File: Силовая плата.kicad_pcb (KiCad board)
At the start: 2 copper layers, 75 x 75 mm, 9 parts, among them Q1 BSP89, Q2 BSP89, Q3 BSP89, Q4 BSP89, Q5 BSP89, Q6 BSP89, U1 HIP2100_SOIC, U2 HIP2100_SOIC, U3 HIP2100_SOIC

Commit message: Вариант с транзисторами в линию
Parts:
- U1, U2, U3: footprint Package_DFN_QFN:DFN-8-1EP_3x3mm_P0.5mm_EP1.65x2.38mm -> Package_SO:SOIC-8_3.9x4.9mm_P1.27mm
- moved U1 118.7 mm to (180.3, 100.3), turned to 90 degrees
- moved U2 90.1 mm to (154.3, 100.3)
- moved U3 75.4 mm to (127.6, 100.3)
- moved Q1 12.3 mm to (133.1, 86.2), turned to -90 degrees
- moved Q3 10.9 mm to (158.1, 86.4), turned to -90 degrees
- moved Q5 10.0 mm to (182.0, 86.2), turned to -90 degrees
- moved Q6 9.01 mm to (170.2, 82.5), turned to 90 degrees
- moved Q4 7.75 mm to (146.1, 82.5), turned to 90 degrees
- moved Q2 6.22 mm to (121.0, 82.5), turned to 90 degrees
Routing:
- net G3: track 0.00 -> 28.1 mm, vias 0 -> 1
- net G1: track 0.00 -> 27.9 mm, vias 0 -> 1
- net G5: track 0.00 -> 24.8 mm, vias 0 -> 1
- net G6: track 0.00 -> 20.0 mm, vias 0 -> 1
- net G4: track 0.00 -> 18.5 mm, vias 0 -> 1
- net G2: track 0.00 -> 17.9 mm, vias 0 -> 1
- net C: vias 0 -> 12
- net B: vias 0 -> 12
- net A: vias 0 -> 12
- net +12V: vias 0 -> 11
- added copper zone on B.Cu, net +12V
- added copper zone on B.Cu, net A
- added copper zone on In1.Cu, net A
- added copper zone on In2.Cu, net A
- added copper zone on In3.Cu, net A
- added copper zone on In4.Cu, net A
- added copper zone on B.Cu, net B
- added copper zone on F.Cu, net B
- added copper zone on In1.Cu, net B
- added copper zone on In2.Cu, net B
- added copper zone on In3.Cu, net B
- added copper zone on In4.Cu, net B
- added copper zone on B.Cu, net C
- added copper zone on F.Cu, net C
- added copper zone on In1.Cu, net C
- added copper zone on In2.Cu, net C
- added copper zone on In3.Cu, net C
- added copper zone on In4.Cu, net C
- added copper zone on In1.Cu, net GND
- added copper zone on In2.Cu, net GND
- added copper zone on In3.Cu, net GND
- added copper zone on In4.Cu, net GND
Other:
- copper layers 2 -> 6

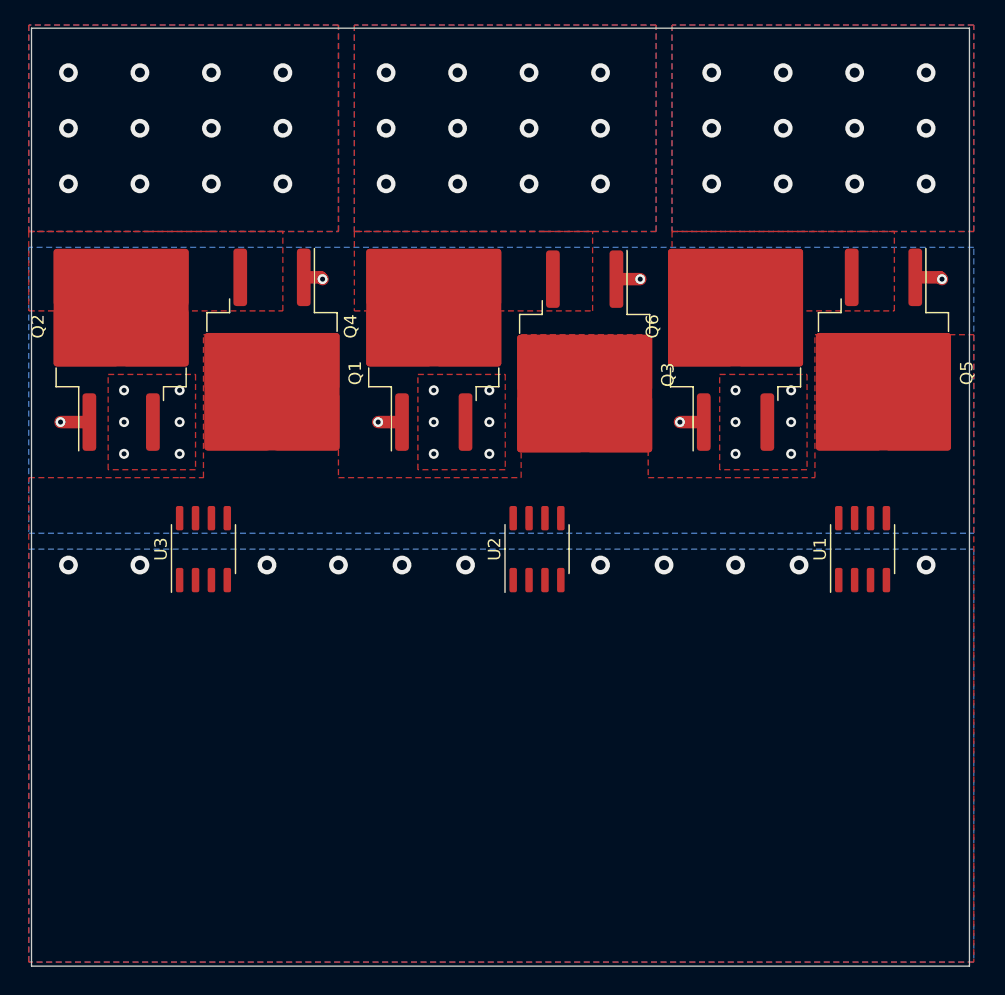
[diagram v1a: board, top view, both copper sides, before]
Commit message: Добавил датчики тока и шунты
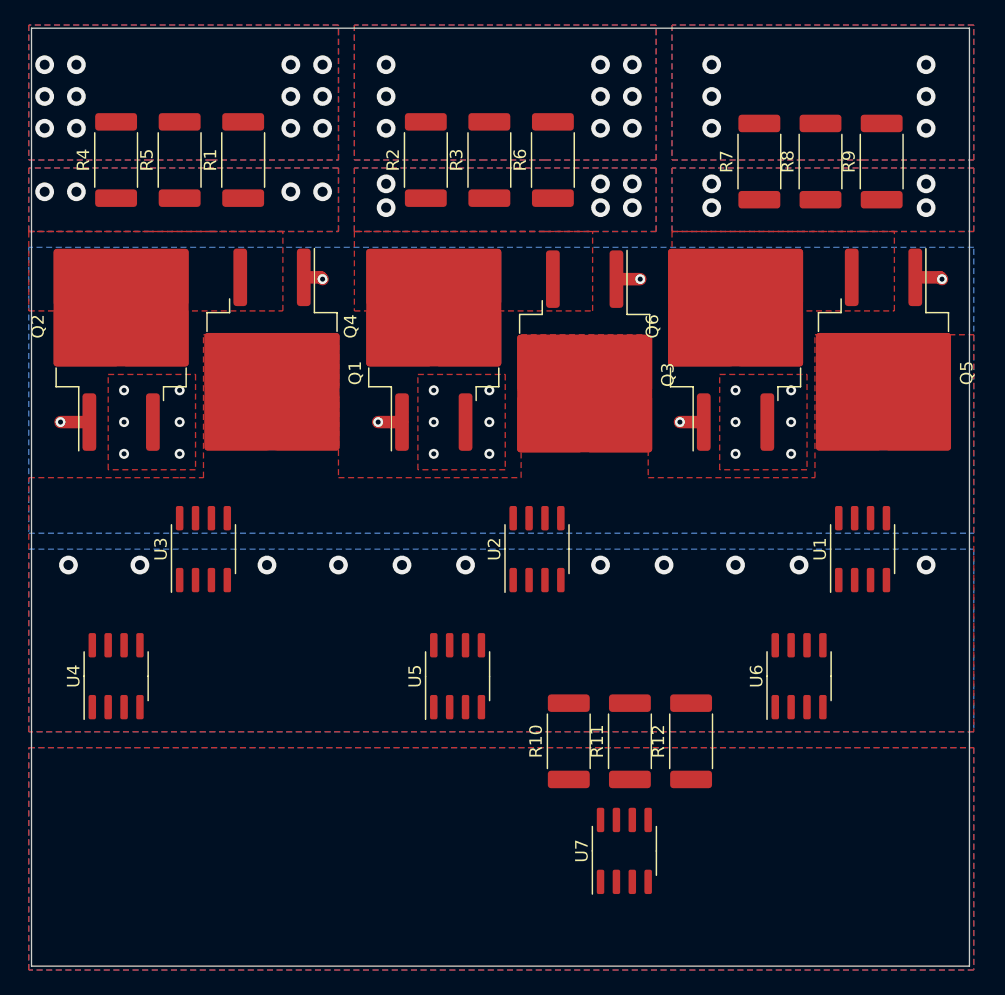
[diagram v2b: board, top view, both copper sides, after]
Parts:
- added R1: R, Resistor_SMD:R_2512_6332Metric_Pad1.40x3.35mm_HandSolder, F.Cu at (130.8, 69.2)
- added R10: R, Resistor_SMD:R_2512_6332Metric_Pad1.40x3.35mm_HandSolder, F.Cu at (156.8, 115.7)
- added R11: R, Resistor_SMD:R_2512_6332Metric_Pad1.40x3.35mm_HandSolder, F.Cu at (161.7, 115.7)
- added R12: R, Resistor_SMD:R_2512_6332Metric_Pad1.40x3.35mm_HandSolder, F.Cu at (166.6, 115.7)
- added R2: R, Resistor_SMD:R_2512_6332Metric_Pad1.40x3.35mm_HandSolder, F.Cu at (145.4, 69.2)
- added R3: R, Resistor_SMD:R_2512_6332Metric_Pad1.40x3.35mm_HandSolder, F.Cu at (150.5, 69.2)
- added R4: R, Resistor_SMD:R_2512_6332Metric_Pad1.40x3.35mm_HandSolder, F.Cu at (120.7, 69.2)
- added R5: R, Resistor_SMD:R_2512_6332Metric_Pad1.40x3.35mm_HandSolder, F.Cu at (125.7, 69.2)
- added R6: R, Resistor_SMD:R_2512_6332Metric_Pad1.40x3.35mm_HandSolder, F.Cu at (155.6, 69.2)
- added R7: R, Resistor_SMD:R_2512_6332Metric_Pad1.40x3.35mm_HandSolder, F.Cu at (172.1, 69.3)
- added R8: R, Resistor_SMD:R_2512_6332Metric_Pad1.40x3.35mm_HandSolder, F.Cu at (177.0, 69.3)
- added R9: R, Resistor_SMD:R_2512_6332Metric_Pad1.40x3.35mm_HandSolder, F.Cu at (181.9, 69.3)
- added U4: AD8210, Package_SO:SOIC-8_3.9x4.9mm_P1.27mm, F.Cu at (120.7, 110.5)
- added U5: AD8210, Package_SO:SOIC-8_3.9x4.9mm_P1.27mm, F.Cu at (148.0, 110.5)
- added U6: AD8210, Package_SO:SOIC-8_3.9x4.9mm_P1.27mm, F.Cu at (175.3, 110.5)
- added U7: AD8210, Package_SO:SOIC-8_3.9x4.9mm_P1.27mm, F.Cu at (161.3, 124.5)
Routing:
- net A2: track 0.00 -> 57.3 mm, vias 0 -> 12
- net B2: track 0.00 -> 54.2 mm, vias 0 -> 9
- net C2: track 0.00 -> 52.0 mm, vias 0 -> 6
- net C: track 0.00 -> 37.0 mm, vias 12 -> 4
- net B: track 0.00 -> 35.9 mm, vias 12 -> 6
- net A: track 0.00 -> 34.2 mm, vias 12 -> 4
- added copper zone on B.Cu, net +12VA
- added copper zone on F.Cu, net +12VA
- added copper zone on B.Cu, net A2
- added copper zone on F.Cu, net A2
- added copper zone on In1.Cu, net A2
- added copper zone on In3.Cu, net A2
- added copper zone on In4.Cu, net A2
- added copper zone on B.Cu, net B2
- added copper zone on F.Cu, net B2
- added copper zone on In1.Cu, net B2
- added copper zone on In3.Cu, net B2
- added copper zone on In4.Cu, net B2
- added copper zone on B.Cu, net C2
- added copper zone on F.Cu, net C2
- added copper zone on In1.Cu, net C2
- added copper zone on In3.Cu, net C2
- added copper zone on In4.Cu, net C2
- removed copper zone on In2.Cu, net A
- removed copper zone on In2.Cu, net B
- removed copper zone on In2.Cu, net C

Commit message: Начальная версия
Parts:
- added C1: 1400m, Capacitor_THT:CP_Axial_L30.0mm_D18.0mm_P35.00mm_Horizontal, F.Cu at (110.8, 68.6)
- added C10: 0.1u, Capacitor_SMD:C_0805_2012Metric_Pad1.18x1.45mm_HandSolder, F.Cu at (47.4, 157.1)
- added C11: 0.1u, Capacitor_SMD:C_0805_2012Metric_Pad1.18x1.45mm_HandSolder, F.Cu at (47.4, 160.1)
- added C12: 0.1u, Capacitor_SMD:C_0805_2012Metric_Pad1.18x1.45mm_HandSolder, F.Cu at (47.4, 163.1)
- added C13: 0.1u, Capacitor_SMD:C_0805_2012Metric_Pad1.18x1.45mm_HandSolder, F.Cu at (47.4, 166.1)
- added C2: 1400m, Capacitor_THT:CP_Axial_L30.0mm_D18.0mm_P35.00mm_Horizontal, F.Cu at (111.0, 88.3)
- added C3: 1400m, Capacitor_THT:CP_Axial_L30.0mm_D18.0mm_P35.00mm_Horizontal, F.Cu at (111.0, 108.7)
- added C4: C_Small, Capacitor_SMD:C_0805_2012Metric_Pad1.18x1.45mm_HandSolder, F.Cu at (136.7, 108.6)
- added C5: BS, Capacitor_SMD:C_0805_2012Metric_Pad1.18x1.45mm_HandSolder, F.Cu at (123.2, 109.2)
- added C6: C_Small, Capacitor_SMD:C_0805_2012Metric_Pad1.18x1.45mm_HandSolder, F.Cu at (161.7, 108.6)
- added C7: BS, Capacitor_SMD:C_0805_2012Metric_Pad1.18x1.45mm_HandSolder, F.Cu at (148.2, 109.2)
- added C8: C_Small, Capacitor_SMD:C_0805_2012Metric_Pad1.18x1.45mm_HandSolder, F.Cu at (186.7, 108.8)
- added C9: BS, Capacitor_SMD:C_0805_2012Metric_Pad1.18x1.45mm_HandSolder, F.Cu at (173.2, 109.0)
- added D1: D_Small, Diode_SMD:D_SOD-323, F.Cu at (130.6, 113.0)
- added D2: D_Small, Diode_SMD:D_SOD-323, F.Cu at (155.6, 113.0)
- added D3: D_Small, Diode_SMD:D_SOD-323, F.Cu at (180.6, 113.2)
- added J6: 2-338069-0, Connector_My:2-338069-0, F.Cu at (138.4, 122.0)
- added R13: 2.7, Resistor_SMD:R_1206_3216Metric_Pad1.30x1.75mm_HandSolder, F.Cu at (117.5, 102.2)
- added R14: 2.7, Resistor_SMD:R_1206_3216Metric_Pad1.30x1.75mm_HandSolder, F.Cu at (123.2, 102.2)
- added R15: 2.7, Resistor_SMD:R_1206_3216Metric_Pad1.30x1.75mm_HandSolder, F.Cu at (142.5, 102.2)
- added R16: 2.7, Resistor_SMD:R_1206_3216Metric_Pad1.30x1.75mm_HandSolder, F.Cu at (148.2, 102.2)
- added R17: 2.7, Resistor_SMD:R_1206_3216Metric_Pad1.30x1.75mm_HandSolder, F.Cu at (167.5, 102.2)
- added R18: 2.7, Resistor_SMD:R_1206_3216Metric_Pad1.30x1.75mm_HandSolder, F.Cu at (173.2, 102.2)
- added R19: 10k, Resistor_SMD:R_0805_2012Metric_Pad1.20x1.40mm_HandSolder, F.Cu at (52.2, 157.1)
- added R20: 10k, Resistor_SMD:R_0805_2012Metric_Pad1.20x1.40mm_HandSolder, F.Cu at (52.2, 160.0)
- U1, U2, U3: value HIP2100_SOIC -> IRS21867S
- moved R3 131.1 mm to (83.8, 182.1)
- moved R4 131.1 mm to (54.0, 182.1)
- moved R5 131.1 mm to (59.1, 182.1)
- moved R7 131.1 mm to (105.4, 182.2)
- moved R9 131.1 mm to (115.2, 182.2)
- moved R1 131.1 mm to (64.1, 182.1)
- moved R2 131.1 mm to (78.7, 182.1)
- moved R6 131.1 mm to (88.9, 182.1)
- moved R8 131.1 mm to (110.3, 182.2)
- moved U3 53.5 mm to (180.4, 108.8), turned to 180 degrees
- moved U1 50.6 mm to (130.4, 108.6), turned to 180 degrees
- moved R10 44.3 mm to (129.5, 150.6)
- moved R11 44.3 mm to (134.4, 150.6)
- moved R12 44.3 mm to (139.3, 150.6)
- moved U5 44.3 mm to (120.7, 145.3)
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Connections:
- Q1 pad 2: +12V -> +24V
- Q3 pad 2: +12V -> +24V
- Q5 pad 2: +12V -> +24V
- R10 pad 1: +12VA -> C
- R10 pad 2: +12V -> C2
- R11 pad 1: +12VA -> C
- R11 pad 2: +12V -> C2
- R12 pad 1: +12VA -> C
- R12 pad 2: +12V -> C2
- R2 pad 1: B -> A
- R2 pad 2: B2 -> A2
- R3 pad 1: B -> A
- R3 pad 2: B2 -> A2
- R4 pad 1: A -> B
- R4 pad 2: A2 -> B2
- R5 pad 1: A -> B
- R5 pad 2: A2 -> B2
- R7 pad 1: C -> +BATT
- R7 pad 2: C2 -> +24V
- R8 pad 1: C -> +BATT
- R8 pad 2: C2 -> +24V
- R9 pad 1: C -> +BATT
- R9 pad 2: C2 -> +24V
- U1 pad 1: unconnected-(U1-VDD-Pad1) -> Net-(D1-A)
- U1 pad 2: unconnected-(U1-HB-Pad2) -> HIN_A
- U1 pad 3: unconnected-(U1-HO-Pad3) -> LIN_A
- U1 pad 4: unconnected-(U1-HS-Pad4) -> Net-(U1-COM)
- U1 pad 5: unconnected-(U1-HI-Pad5) -> Net-(U1-LO)
- U1 pad 6: unconnected-(U1-LI-Pad6) -> Net-(U1-VS)
- U1 pad 7: unconnected-(U1-VSS-Pad7) -> Net-(U1-HO)
- U1 pad 8: unconnected-(U1-LO-Pad8) -> Net-(D1-K)
- U2 pad 1: unconnected-(U2-VDD-Pad1) -> Net-(D2-A)
- U2 pad 2: unconnected-(U2-HB-Pad2) -> HIN_B
- U2 pad 3: unconnected-(U2-HO-Pad3) -> LIN_B
- U2 pad 4: unconnected-(U2-HS-Pad4) -> Net-(U2-COM)
- U2 pad 5: unconnected-(U2-HI-Pad5) -> Net-(U2-LO)
- U2 pad 6: unconnected-(U2-LI-Pad6) -> Net-(U2-VS)
- U2 pad 7: unconnected-(U2-VSS-Pad7) -> Net-(U2-HO)
- U2 pad 8: unconnected-(U2-LO-Pad8) -> Net-(D2-K)
- U3 pad 1: unconnected-(U3-VDD-Pad1) -> Net-(D3-A)
- U3 pad 2: unconnected-(U3-HB-Pad2) -> HIN_C
- U3 pad 3: unconnected-(U3-HO-Pad3) -> LIN_C
- U3 pad 4: unconnected-(U3-HS-Pad4) -> Net-(U3-COM)
- U3 pad 5: unconnected-(U3-HI-Pad5) -> Net-(U3-LO)
- U3 pad 6: unconnected-(U3-LI-Pad6) -> Net-(U3-VS)
- U3 pad 7: unconnected-(U3-VSS-Pad7) -> Net-(U3-HO)
- U3 pad 8: unconnected-(U3-LO-Pad8) -> Net-(D3-K)
- U4 pad 3: unconnected-(U4-Vref2-Pad3) -> Vref
- U4 pad 5: unconnected-(U4-OUT-Pad5) -> Current_A
- U4 pad 6: unconnected-(U4-V+-Pad6) -> +5V
- U4 pad 7: unconnected-(U4-Vref1-Pad7) -> Vref
- U5 pad 3: unconnected-(U5-Vref2-Pad3) -> Vref
- U5 pad 5: unconnected-(U5-OUT-Pad5) -> Current_B
- U5 pad 6: unconnected-(U5-V+-Pad6) -> +5V
- U5 pad 7: unconnected-(U5-Vref1-Pad7) -> Vref
- U6 pad 1: C2 -> +24V
- U6 pad 3: unconnected-(U6-Vref2-Pad3) -> GND
- U6 pad 5: unconnected-(U6-OUT-Pad5) -> DC_Measure
- U6 pad 6: unconnected-(U6-V+-Pad6) -> +5V
- U6 pad 7: unconnected-(U6-Vref1-Pad7) -> +5V
- U6 pad 8: C -> +BATT
- U7 pad 1: +12V -> C2
- U7 pad 3: unconnected-(U7-Vref2-Pad3) -> Vref
- U7 pad 5: unconnected-(U7-OUT-Pad5) -> Current_C
- U7 pad 6: unconnected-(U7-V+-Pad6) -> +5V
- U7 pad 7: unconnected-(U7-Vref1-Pad7) -> Vref
- U7 pad 8: +12VA -> C
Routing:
- net A2: track 57.3 -> 0.00 mm, vias 12 -> 0
- net B2: track 54.2 -> 0.00 mm, vias 9 -> 0
- net C2: track 52.0 -> 0.00 mm, vias 6 -> 0
- net C: track 37.0 -> 0.00 mm, vias 4 -> 8
- net B: track 35.9 -> 0.00 mm, vias 6 -> 8
- net A: track 34.2 -> 0.00 mm, vias 4 -> 8
- net G3: track 28.1 -> 0.00 mm, vias 1 -> 0
- net G1: track 27.9 -> 0.00 mm, vias 1 -> 0
- net G5: track 24.8 -> 0.00 mm, vias 1 -> 0
- net G6: track 20.0 -> 0.00 mm, vias 1 -> 0
- net G4: track 18.5 -> 0.00 mm, vias 1 -> 0
- net G2: track 17.9 -> 0.00 mm, vias 1 -> 0
- net GND: vias 18 -> 54
- net +24V: vias 0 -> 24
- net +12V: vias 11 -> 0
- added copper zone on B.Cu, net +24V
- added copper zone on F.Cu, net +24V
- added copper zone on In4.Cu, net +24V
- removed copper zone on B.Cu, net +12V
- removed copper zone on F.Cu, net +12V
- removed copper zone on B.Cu, net +12VA
- removed copper zone on F.Cu, net +12VA
- removed copper zone on In1.Cu, net A
- removed copper zone on In3.Cu, net A
- removed copper zone on In4.Cu, net A
- removed copper zone on B.Cu, net A2
- removed copper zone on F.Cu, net A2
- removed copper zone on In1.Cu, net A2
- removed copper zone on In3.Cu, net A2
- removed copper zone on In4.Cu, net A2
- removed copper zone on In1.Cu, net B
- removed copper zone on In3.Cu, net B
- removed copper zone on In4.Cu, net B
- removed copper zone on B.Cu, net B2
- removed copper zone on F.Cu, net B2
- removed copper zone on In1.Cu, net B2
- removed copper zone on In3.Cu, net B2
- removed copper zone on In4.Cu, net B2
- removed copper zone on In1.Cu, net C
- removed copper zone on In3.Cu, net C
- removed copper zone on In4.Cu, net C
- removed copper zone on B.Cu, net C2
- removed copper zone on F.Cu, net C2
- removed copper zone on In1.Cu, net C2
- removed copper zone on In3.Cu, net C2
- removed copper zone on In4.Cu, net C2
- removed copper zone on In1.Cu, net GND
- removed copper zone on In2.Cu, net GND
- removed copper zone on In3.Cu, net GND
- removed copper zone on In4.Cu, net GND
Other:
- board size 75 x 75 mm -> 75 x 66.7 mm

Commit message: Стартовый вариант
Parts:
- removed C10, C11, C12, C13: 0.1u, Capacitor_SMD:C_0805_2012Metric_Pad1.18x1.45mm_HandSolder
- removed C2, C3: 1400m, Capacitor_THT:CP_Axial_L30.0mm_D18.0mm_P35.00mm_Horizontal
- removed R1, R10, R11, R12, R2, R3, R4, R5, R6, R7, R8, R9: R, Resistor_SMD:R_2512_6332Metric_Pad1.40x3.35mm_HandSolder
- removed R19, R20: 10k, Resistor_SMD:R_0805_2012Metric_Pad1.20x1.40mm_HandSolder
- removed U4, U5, U6, U7: AD8210, Package_SO:SOIC-8_3.9x4.9mm_P1.27mm
- added C14: 4.7u, Capacitor_SMD:C_1206_3216Metric_Pad1.33x1.80mm_HandSolder, F.Cu at (177.8, 113.0)
- added C15: 4.7u, Capacitor_SMD:C_1206_3216Metric_Pad1.33x1.80mm_HandSolder, F.Cu at (177.8, 109.9)
- added C16: 4.7u, Capacitor_SMD:C_1206_3216Metric_Pad1.33x1.80mm_HandSolder, F.Cu at (127.3, 108.0)
- added C17: 4.7u, Capacitor_SMD:C_1206_3216Metric_Pad1.33x1.80mm_HandSolder, F.Cu at (127.3, 111.1)
- added C18: 4.7u, Capacitor_SMD:C_1206_3216Metric_Pad1.33x1.80mm_HandSolder, F.Cu at (127.3, 114.3)
- added C19: 4.7u, Capacitor_SMD:C_1206_3216Metric_Pad1.33x1.80mm_HandSolder, F.Cu at (127.3, 117.5)
- added C20: 4.7u, Capacitor_SMD:C_1206_3216Metric_Pad1.33x1.80mm_HandSolder, F.Cu at (133.0, 104.8)
- added C21: 4.7u, Capacitor_SMD:C_1206_3216Metric_Pad1.33x1.80mm_HandSolder, F.Cu at (133.0, 114.3)
- added C22: 4.7u, Capacitor_SMD:C_1206_3216Metric_Pad1.33x1.80mm_HandSolder, F.Cu at (133.0, 111.1)
- added C23: 4.7u, Capacitor_SMD:C_1206_3216Metric_Pad1.33x1.80mm_HandSolder, F.Cu at (133.0, 108.0)
- added C24: 4.7u, Capacitor_SMD:C_1206_3216Metric_Pad1.33x1.80mm_HandSolder, F.Cu at (184.2, 109.9)
- added C25: 4.7u, Capacitor_SMD:C_1206_3216Metric_Pad1.33x1.80mm_HandSolder, F.Cu at (184.2, 113.0)
- added C26: 4.7u, Capacitor_SMD:C_1206_3216Metric_Pad1.33x1.80mm_HandSolder, F.Cu at (184.2, 116.2)
- added C27: 4.7u, Capacitor_SMD:C_1206_3216Metric_Pad1.33x1.80mm_HandSolder, F.Cu at (184.2, 119.4)
- added C28: 4.7u, Capacitor_SMD:C_1206_3216Metric_Pad1.33x1.80mm_HandSolder, F.Cu at (177.8, 116.2)
- added C29: 4.7u, Capacitor_SMD:C_1206_3216Metric_Pad1.33x1.80mm_HandSolder, F.Cu at (184.2, 94.0)
- added C30: 4.7u, Capacitor_SMD:C_1206_3216Metric_Pad1.33x1.80mm_HandSolder, F.Cu at (184.2, 97.2)
- added C31: 4.7u, Capacitor_SMD:C_1206_3216Metric_Pad1.33x1.80mm_HandSolder, F.Cu at (184.2, 100.3)
- added C32: 4.7u, Capacitor_SMD:C_1206_3216Metric_Pad1.33x1.80mm_HandSolder, F.Cu at (184.2, 103.5)
- added C33: 4.7u, Capacitor_SMD:C_1206_3216Metric_Pad1.33x1.80mm_HandSolder, F.Cu at (184.2, 106.7)
- added C34: 4.7u, Capacitor_SMD:C_1206_3216Metric_Pad1.33x1.80mm_HandSolder, F.Cu at (121.9, 117.5)
- added C35: 4.7u, Capacitor_SMD:C_1206_3216Metric_Pad1.33x1.80mm_HandSolder, F.Cu at (121.9, 114.3)
- added C36: 4.7u, Capacitor_SMD:C_1206_3216Metric_Pad1.33x1.80mm_HandSolder, F.Cu at (121.9, 111.1)
- added C37: 4.7u, Capacitor_SMD:C_1206_3216Metric_Pad1.33x1.80mm_HandSolder, F.Cu at (121.9, 108.0)
- added C38: 4.7u, Capacitor_SMD:C_1206_3216Metric_Pad1.33x1.80mm_HandSolder, F.Cu at (121.9, 104.8)
- added C39: 4.7u, Capacitor_SMD:C_1206_3216Metric_Pad1.33x1.80mm_HandSolder, F.Cu at (121.9, 96.5)
- added C40: 4.7u, Capacitor_SMD:C_1206_3216Metric_Pad1.33x1.80mm_HandSolder, F.Cu at (121.9, 93.3)
- added C41: 4.7u, Capacitor_SMD:C_1206_3216Metric_Pad1.33x1.80mm_HandSolder, F.Cu at (121.9, 90.5)
- added C42: 4.7u, Capacitor_SMD:C_1206_3216Metric_Pad1.33x1.80mm_HandSolder, F.Cu at (121.9, 87.1)
- added C43: 4.7u, Capacitor_SMD:C_1206_3216Metric_Pad1.33x1.80mm_HandSolder, F.Cu at (121.9, 83.8)
- added C44: 4.7u, Capacitor_SMD:C_1206_3216Metric_Pad1.33x1.80mm_HandSolder, F.Cu at (177.8, 106.7)
- added C45: 4.7u, Capacitor_SMD:C_1206_3216Metric_Pad1.33x1.80mm_HandSolder, F.Cu at (171.4, 113.0)
- added C46: 4.7u, Capacitor_SMD:C_1206_3216Metric_Pad1.33x1.80mm_HandSolder, F.Cu at (171.4, 109.9)
- added C47: 4.7u, Capacitor_SMD:C_1206_3216Metric_Pad1.33x1.80mm_HandSolder, F.Cu at (171.4, 106.7)
- added C48: 4.7u, Capacitor_SMD:C_1206_3216Metric_Pad1.33x1.80mm_HandSolder, F.Cu at (171.4, 116.2)
- added J1: Conn_01x01, Connector_My:Power_Wire, F.Cu at (133.3, 113.5)
- added J2: Conn_01x01, Connector_My:Power_Wire, F.Cu at (171.4, 113.5)
- added J3: Conn_01x01, Connector_My:Power_Wire, F.Cu at (132.7, 45.6)
- added J4: Conn_01x01, Connector_My:Power_Wire, F.Cu at (152.4, 45.6)
- added J5: Conn_01x01, Connector_My:Power_Wire, F.Cu at (172.1, 45.6)
- C1: footprint Capacitor_THT:CP_Axial_L30.0mm_D18.0mm_P35.00mm_Horizontal -> Capacitor_THT:CP_Axial_L18.0mm_D8.0mm_P25.00mm_Horizontal
- moved C1 56.9 mm to (139.9, 117.5), turned to 0 degrees
- moved C8 25.6 mm to (162.6, 100.3), turned to 90 degrees
- moved Q1 22.7 mm to (131.4, 88.3), turned to 180 degrees
- moved R13 21.7 mm to (138.4, 96.5)
- moved Q5 21.6 mm to (169.5, 88.3), turned to 180 degrees
- moved Q3 21.4 mm to (150.6, 88.3), turned to 180 degrees
- moved D3 20.7 mm to (168.3, 96.5), turned to 180 degrees
- moved C6 20.0 mm to (143.5, 100.3), turned to 90 degrees
- moved R14 18.7 mm to (141.0, 96.5)
- moved D2 17.7 mm to (149.2, 96.5), turned to 180 degrees
- moved C5 17.5 mm to (135.3, 96.5), turned to 0 degrees
- moved D1 16.5 mm to (130.2, 96.5), turned to 180 degrees
- moved R15 16.1 mm to (157.5, 96.5)
- moved U3 14.8 mm to (168.3, 100.3), turned to 0 degrees
- moved C4 14.8 mm to (124.5, 100.3), turned to 90 degrees
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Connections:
- J6 pad 1: unconnected-(J6-Pad1) -> HIN_A
- J6 pad 10: unconnected-(J6-Pad10) -> LIN_B
- J6 pad 11: unconnected-(J6-Pad11) -> HIN_B
- J6 pad 19: unconnected-(J6-Pad19) -> LIN_C
- J6 pad 2: unconnected-(J6-Pad2) -> LIN_A
- J6 pad 20: unconnected-(J6-Pad20) -> HIN_C
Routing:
- net GND: track 0.00 -> 118.5 mm, vias 54 -> 50
- net HIN_A: track 0.00 -> 25.0 mm, vias 0 -> 2
- net LIN_A: track 0.00 -> 24.3 mm, vias 0 -> 2
- net G2: track 0.00 -> 17.7 mm, vias 0 -> 2
- net G6: track 0.00 -> 17.7 mm, vias 0 -> 2
- net G4: track 0.00 -> 17.6 mm, vias 0 -> 2
- net HIN_C: track 0.00 -> 16.5 mm, vias 0 -> 2
- net LIN_B: track 0.00 -> 16.2 mm, vias 0 -> 2
- net HIN_B: track 0.00 -> 15.3 mm, vias 0 -> 2
- net Net-(U2-LO): track 0.00 -> 10.0 mm
- net Net-(U3-LO): track 0.00 -> 10.0 mm
- net Net-(U1-LO): track 0.00 -> 10.0 mm
- net LIN_C: track 0.00 -> 9.64 mm, vias 0 -> 2
- net Net-(U2-VS): track 0.00 -> 7.48 mm, vias 0 -> 2
- net Net-(U1-VS): track 0.00 -> 7.48 mm, vias 0 -> 2
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- added copper zone on In1.Cu, net +24V
- added copper zone on In1.Cu, net A
- added copper zone on In2.Cu, net A
- added copper zone on In3.Cu, net A
- added copper zone on In4.Cu, net A
- added copper zone on In1.Cu, net B
- added copper zone on In2.Cu, net B
- added copper zone on In3.Cu, net B
- added copper zone on In4.Cu, net B
- added copper zone on In1.Cu, net C
- added copper zone on In2.Cu, net C
- added copper zone on In3.Cu, net C
- added copper zone on In4.Cu, net C
- added copper zone on In2.Cu, net GND
- removed copper zone on In4.Cu, net +24V
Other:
- board size 75 x 66.7 mm -> 68 x 66.7 mm
